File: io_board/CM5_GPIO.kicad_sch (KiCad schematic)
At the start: 21 parts, among them J14 JST_SHBM04B-SRSS-TB, J2 Conn_02x07_Odd_Even, J3 Conn_01x03, J7 Micro_SD_Card_Det, J8 THD-20-R, SW1 Right angle Tact button, U18 RT9742GGJ5

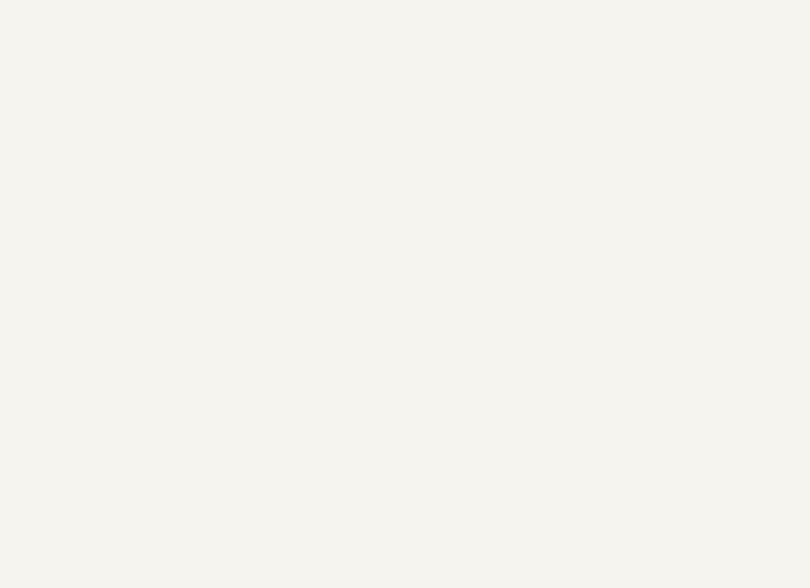
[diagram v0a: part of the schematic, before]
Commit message: Added all necessary IO connectors.
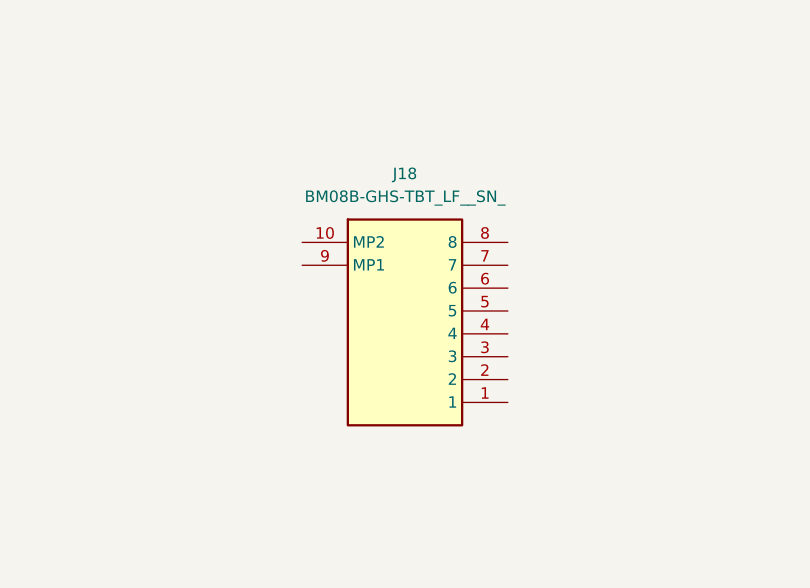
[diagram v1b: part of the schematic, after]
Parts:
- added J18: BM08B-GHS-TBT_LF__SN_, BM08B-GHS-TBT_LF__SN_:BM08BGHSTBTLFSN, symbol BM08B-GHS-TBT_LF__SN_:BM08B-GHS-TBT_LF__SN_
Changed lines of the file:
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@@
+	)
+	(symbol
+		(lib_id "BM08B-GHS-TBT_LF__SN_:BM08B-GHS-TBT_LF__SN_")
+		(at 223.52 45.72 0)
+		(unit 1)
+		(exclude_from_sim no)
+		(in_bom yes)
+		(on_board yes)
+		(dnp no)
+		(fields_autoplaced yes)
+		(property "Reference" "J18"
+			(at 234.95 38.1 0)
+			(effects
+				(font
+					(size 1.27 1.27)
+				)
+			)
+		)
+		(property "Value" "BM08B-GHS-TBT_LF__SN_"
+			(at 234.95 40.64 0)
+			(effects
+				(font
+					(size 1.27 1.27)
+				)
+			)
+		)
+		(property "Footprint" "BM08B-GHS-TBT_LF__SN_:BM08BGHSTBTLFSN"
+			(at 242.57 140.64 0)
+			(effects
+				(font
+					(size 1.27 1.27)
+				)
+				(justify left top)
+				(hide yes)
+			)
+		)
+		(property "Datasheet" "https://www.mouser.fr/datasheet/2/564/eGH-3476874.pdf"
+			(at 242.57 240.64 0)
+			(effects
+				(font
+					(size 1.27 1.27)
+				)
+				(justify left top)
+				(hide yes)
+			)
+		)
+		(property "Description" "JST GH Series, 1.25mm Pitch 8 Way Straight PCB Header, Solder Termination, 1A , 50V , -25C ~ 85C"
+			(at 223.52 45.72 0)
+			(effects
+				(font
+					(size 1.27 1.27)
+				)
+				(hide yes)
+			)
+		)
+		(property "Height" "4.2"
+			(at 242.57 440.64 0)
+			(effects
+				(font
+					(size 1.27 1.27)
+				)
+				(justify left top)
+				(hide yes)
+			)
+		)
+		(property "Mouser Part Number" "306-BM08BGHSTBTLFSNN"
+			(at 242.57 540.64 0)
+			(effects
+				(font
+					(size 1.27 1.27)
+				)
+				(justify left top)
+				(hide yes)
+			)
+		)
+		(property "Mouser Price/Stock" "https://www.mouser.co.uk/ProductDetail/JST-Commercial/BM08B-GHS-TBTLFSN?qs=cdbOS8ANM9BgERo6NlzSZA%3D%3D"
+			(at 242.57 640.64 0)
+			(effects
+				(font
+					(size 1.27 1.27)
+				)
+				(justify left top)
+				(hide yes)
+			)
+		)
+		(property "Manufacturer_Name" "JST (JAPAN SOLDERLESS TERMINALS)"
+			(at 242.57 740.64 0)
+			(effects
+				(font
+					(size 1.27 1.27)
+				)
+				(justify left top)
+				(hide yes)
+			)
+		)
+		(property "Manufacturer_Part_Number" "BM08B-GHS-TBT(LF)(SN)"
+			(at 242.57 840.64 0)
+			(effects
+				(font
+					(size 1.27 1.27)
+				)
+				(justify left top)
+				(hide yes)
+			)
+		)
+		(pin "8"
+		)
+		(pin "5"
+		)
+		(pin "9"
+		)
+		(pin "6"
+		)
+		(pin "10"
+		)
+		(pin "3"
+		)
+		(pin "2"
+		)
+		(pin "1"
+		)
+		(pin "4"
+		)
+		(pin "7"
+		)
+		(instances
+			(project "CM5IO"
+				(path "/e63e39d7-6ac0-4ffd-8aa3-1841a4541b55/00000000-0000-0000-0000-00005cff706a"
+					(reference "J18")
+					(unit 1)
+				)
+			)
+		)
 	)
 	(symbol

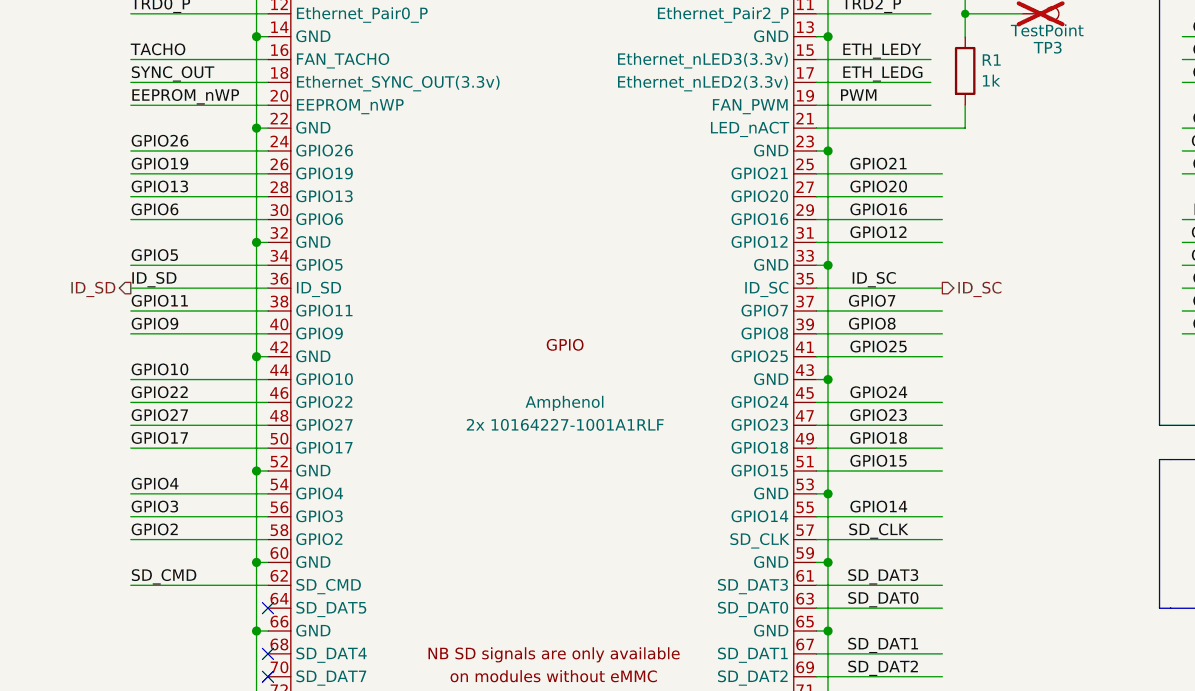
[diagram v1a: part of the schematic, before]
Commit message: Assigned pins to I2C, UART, PWM, SPI ports.
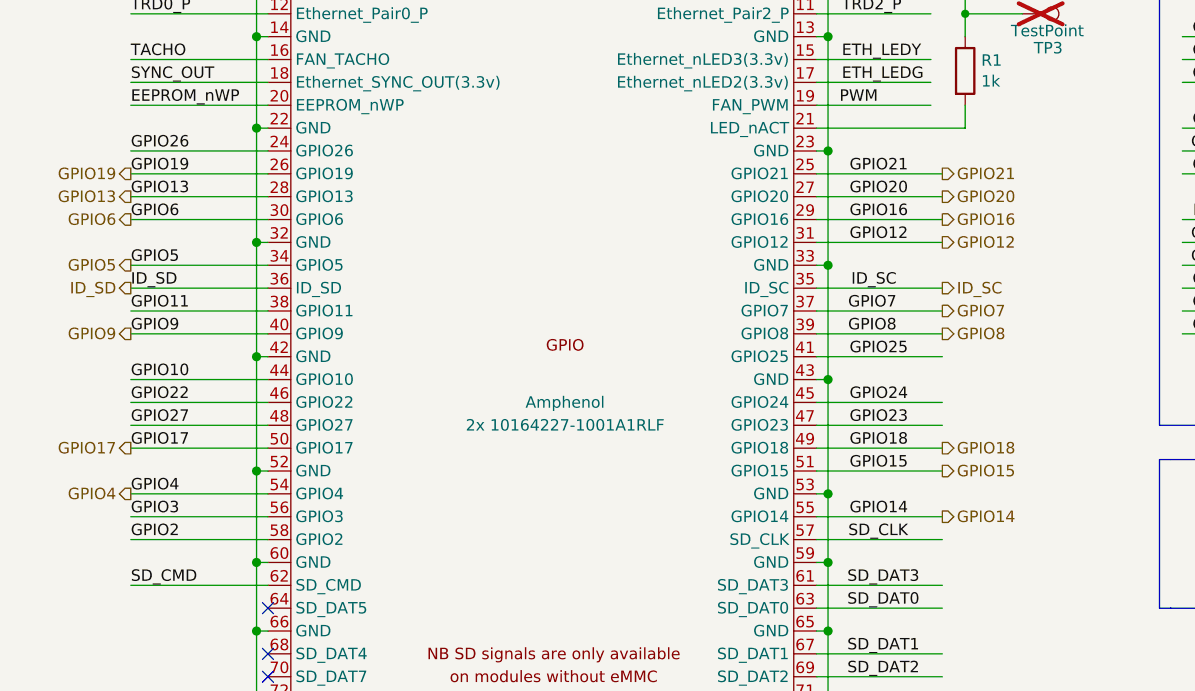
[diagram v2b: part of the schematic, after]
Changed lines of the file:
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@@
+		)
+	)
+	(hierarchical_label "GPIO19"
+		(shape output)
+		(at 24.13 52.07 180)
+		(effects
+			(font
+				(size 1.27 1.27)
+			)
+			(justify right)
 		)
 	)
@@
 		)
 	)
+	(hierarchical_label "GPIO20"
+		(shape output)
+		(at 114.3 54.61 0)
+		(effects
+			(font
+				(size 1.27 1.27)
+			)
+			(justify left)
+		)
+	)
 	(hierarchical_label "ID_SD"
 		(shape output)
@@
 		)
 	)
+	(hierarchical_label "GPIO5"
+		(shape output)
+		(at 24.13 62.23 180)
+		(effects
+			(font
+				(size 1.27 1.27)
+			)
+			(justify right)
+		)
+	)
 	(hierarchical_label "CAM_GPIO1"
 		(shape output)
@@
 		)
 	)
+	(hierarchical_label "GPIO7"
+		(shape output)
+		(at 114.3 67.31 0)
+		(effects
+			(font
+				(size 1.27 1.27)
+			)
+			(justify left)
+		)
+	)
 	(hierarchical_label "CC2"
 		(shape output)
@@
 		)
 	)
+	(hierarchical_label "GPIO18"
+		(shape output)
+		(at 114.3 82.55 0)
+		(effects
+			(font
+				(size 1.27 1.27)
+			)
+			(justify left)
+		)
+	)
+	(hierarchical_label "GPIO15"
+		(shape output)
+		(at 114.3 85.09 0)
+		(effects
+			(font
+				(size 1.27 1.27)
+			)
+			(justify left)
+		)
+	)
 	(hierarchical_label "SCL0"
 		(shape output)
@@
 		)
 	)
+	(hierarchical_label "GPIO17"
+		(shape output)
+		(at 24.13 82.55 180)
+		(effects
+			(font
+				(size 1.27 1.27)
+			)
+			(justify right)
+		)
+	)
+	(hierarchical_label "GPIO12"
+		(shape output)
+		(at 114.3 59.69 0)
+		(effects
+			(font
+				(size 1.27 1.27)
+			)
+			(justify left)
+		)
+	)
+	(hierarchical_label "GPIO9"
+		(shape output)
+		(at 24.13 69.85 180)
+		(effects
+			(font
+				(size 1.27 1.27)
+			)
+			(justify right)
+		)
+	)
 	(hierarchical_label "CAM_GPIO0"
 		(shape output)
 		(at 116.84 143.51 0)
+		(effects
+			(font
+				(size 1.27 1.27)
+			)
+			(justify left)
+		)
+	)
+	(hierarchical_label "GPIO4"
+		(shape output)
+		(at 24.13 87.63 180)
+		(effects
+			(font
+				(size 1.27 1.27)
+			)
+			(justify right)
+		)
+	)
+	(hierarchical_label "GPIO21"
+		(shape output)
+		(at 114.3 52.07 0)
+		(effects
+			(font
+				(size 1.27 1.27)
+			)
+			(justify left)
+		)
+	)
+	(hierarchical_label "GPIO16"
+		(shape output)
+		(at 114.3 57.15 0)
 		(effects
 			(font
@@
 		(effects
 			(font
+				(size 1.27 1.27)
+			)
+			(justify left)
+		)
+	)
+	(hierarchical_label "GPIO14"
+		(shape output)
+		(at 114.3 90.17 0)
+		(effects
+			(font
+				(size 1.27 1.27)
+			)
+			(justify left)
+		)
+	)
+	(hierarchical_label "GPIO6"
+		(shape output)
+		(at 24.13 57.15 180)
+		(effects
+			(font
+				(size 1.27 1.27)
+			)
+			(justify right)
+		)
+	)
+	(hierarchical_label "GPIO13"
+		(shape output)
+		(at 24.13 54.61 180)
+		(effects
+			(font
+				(size 1.27 1.27)
+			)
+			(justify right)
+		)
+	)
+	(hierarchical_label "GPIO8"
+		(shape output)
+		(at 114.3 69.85 0)
+		(effects
+			(font

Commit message: Connected USB 3.0 and added part number for PCIe.
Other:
- company: Copyright © 2024 Raspberry Pi Ltd. -> Copyright © 2024 Raspberry Pi Ltd. & Ilias Kringos
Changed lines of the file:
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@@
 		(title "Compute Module 5 IO Board - GPIO - Ethernet")
 		(rev "1")
-		(company "Copyright © 2024 Raspberry Pi Ltd.")
+		(company "Copyright © 2024 Raspberry Pi Ltd. & Ilias Kringos")
 		(comment 1 "www.raspberrypi.com")
 	)
